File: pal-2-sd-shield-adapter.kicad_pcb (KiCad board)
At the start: 2 copper layers, 24.4 x 41.7 mm, 2 parts, among them J1 Conn_02x13_Odd_Even, J2 Conn_02x09_Odd_Even

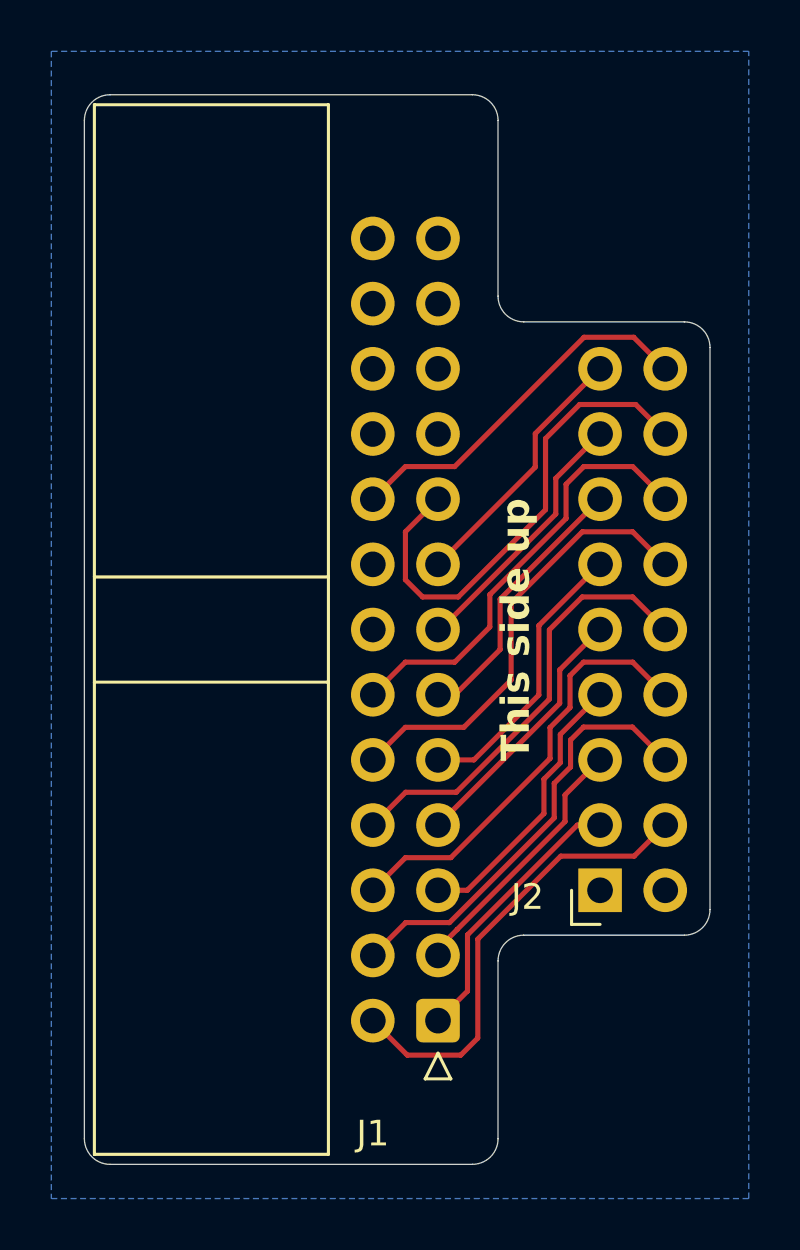
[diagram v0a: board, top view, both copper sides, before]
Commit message: Curved tracks. Works with PAL-I too
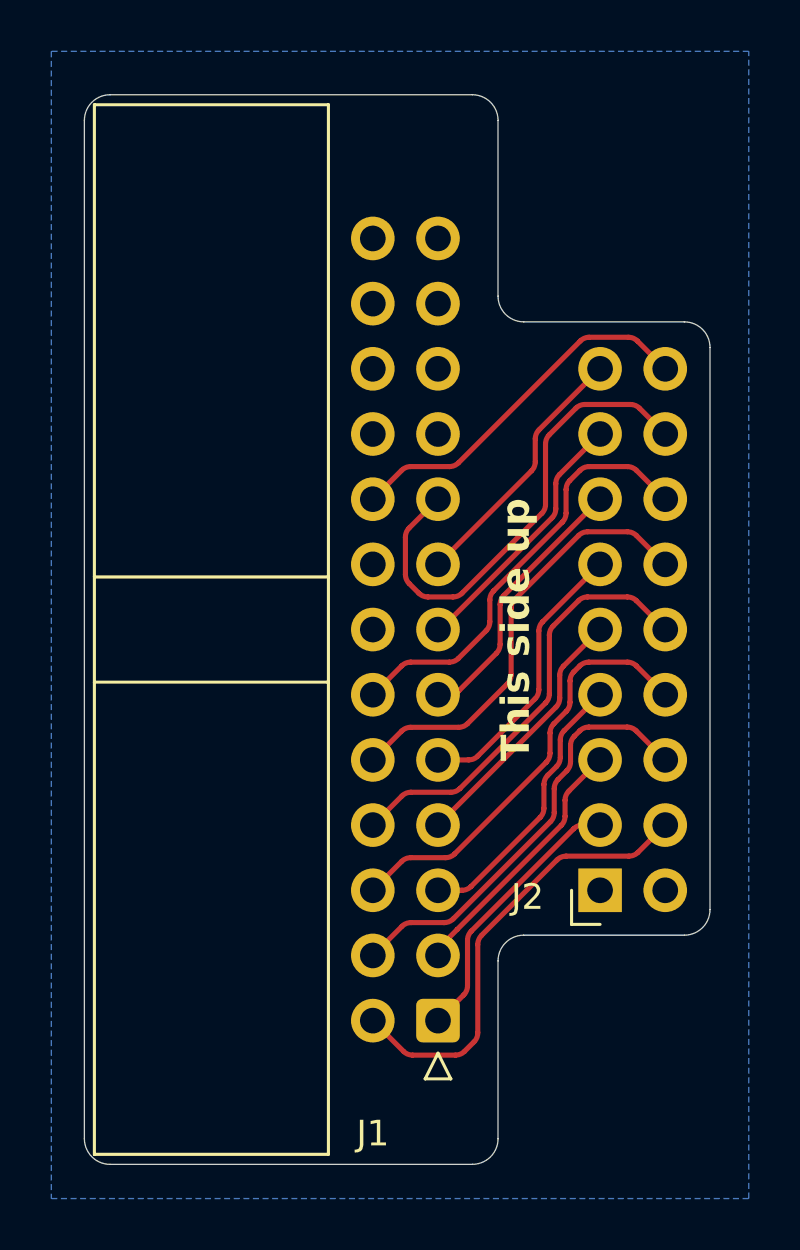
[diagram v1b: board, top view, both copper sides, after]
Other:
- board text added: "PAL-I/II to SD Shield adapter https://github.com/eduardocasino"
- board text removed: "PAL-II to SD Shield adapter https://github.com/eduardocasino"
